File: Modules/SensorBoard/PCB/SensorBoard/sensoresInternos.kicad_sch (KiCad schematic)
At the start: 0 parts

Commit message: sensor board basic components
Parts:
- added U2: BMI160, Package_LGA:Bosch_LGA-14_3x2.5mm_P0.5mm, symbol Sensor_Motion:BMI160
- added U3: BME280, Package_LGA:Bosch_LGA-8_2.5x2.5mm_P0.65mm_ClockwisePinNumbering, symbol Sensor:BME280
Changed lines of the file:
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@@
 (kicad_sch
-	(version 20231120)
+	(version 20250114)
 	(generator "eeschema")
-	(generator_version "8.0")
+	(generator_version "9.0")
 	(paper "A4")
+	(symbol
+		(lib_id "Sensor:BME280")
+		(at 119.38 129.54 0)
+		(unit 1)
+		(exclude_from_sim no)
+		(in_bom yes)
+		(on_board yes)
+		(dnp no)
+		(fields_autoplaced yes)
+		(property "Reference" "U3"
+			(at 107.95 128.2699 0)
+			(effects
+				(font
+					(size 1.27 1.27)
+				)
+				(justify right)
+			)
+		)
+		(property "Value" "BME280"
+			(at 107.95 130.8099 0)
+			(effects
+				(font
+					(size 1.27 1.27)
+				)
+				(justify right)
+			)
+		)
+		(property "Footprint" "Package_LGA:Bosch_LGA-8_2.5x2.5mm_P0.65mm_ClockwisePinNumbering"
+			(at 157.48 140.97 0)
+			(effects
+				(font
+					(size 1.27 1.27)
+				)
+				(hide yes)
+			)
+		)
+		(property "Datasheet" "https://www.bosch-sensortec.com/media/boschsensortec/downloads/datasheets/bst-bme280-ds002.pdf"
+			(at 119.38 134.62 0)
+			(effects
+				(font
+					(size 1.27 1.27)
+				)
+				(hide yes)
+			)
+		)
+		(property "Description" "3-in-1 sensor, humidity, pressure, temperature, I2C and SPI interface, 1.71-3.6V, LGA-8"
+			(at 119.38 129.54 0)
+			(effects
+				(font
+					(size 1.27 1.27)
+				)
+				(hide yes)
+			)
+		)
+		(pin "3"
+		)
+		(pin "2"
+		)
+		(pin "7"
+		)
+		(pin "8"
+		)
+		(pin "1"
+		)
+		(pin "4"
+		)
+		(pin "5"
+		)
+		(pin "6"
+		)
+		(instances
+			(project ""
+				(path "/fa219048-dcb4-48ee-a6b6-8b1fad43a054/b6d62be8-6230-46e7-ab2b-f5043389658b"
+					(reference "U3")
+					(unit 1)
+				)
+			)
+		)
+	)
+	(symbol
+		(lib_id "Sensor_Motion:BMI160")
+		(at 120.65 67.31 0)
+		(unit 1)
+		(exclude_from_sim no)
+		(in_bom yes)
+		(on_board yes)
+		(dnp no)
+		(fields_autoplaced yes)
+		(property "Reference" "U2"
+			(at 122.7933 54.61 0)
+			(effects
+				(font
+					(size 1.27 1.27)
+				)
+				(justify left)
+			)
+		)
+		(property "Value" "BMI160"
+			(at 122.7933 57.15 0)
+			(effects
+				(font
+					(size 1.27 1.27)
+				)
+				(justify left)
+			)
+		)
+		(property "Footprint" "Package_LGA:Bosch_LGA-14_3x2.5mm_P0.5mm"
+			(at 120.65 67.31 0)
+			(effects
+				(font
+					(size 1.27 1.27)
+				)
+				(hide yes)
+			)
+		)
+		(property "Datasheet" "https://www.bosch-sensortec.com/media/boschsensortec/downloads/datasheets/bst-bmi160-ds000.pdf"
+			(at 102.87 45.72 0)
+			(effects
+				(font
+					(size 1.27 1.27)
+				)
+				(hide yes)
+			)
+		)
+		(property "Description" "Small, low power inertial measurement unit, LGA-14"
+			(at 120.65 67.31 0)
+			(effects
+				(font
+					(size 1.27 1.27)
+				)
+				(hide yes)
+			)
+		)
+		(pin "12"
+		)
+		(pin "3"
+		)
+		(pin "7"
+		)
+		(pin "4"
+		)
+		(pin "8"
+		)
+		(pin "1"
+		)
+		(pin "9"
+		)
+		(pin "11"
+		)
+		(pin "10"
+		)
+		(pin "6"
+		)
+		(pin "5"
+		)
+		(pin "2"
+		)
+		(pin "14"
+		)
+		(pin "13"
+		)
+		(instances
+			(project ""
+				(path "/fa219048-dcb4-48ee-a6b6-8b1fad43a054/b6d62be8-6230-46e7-ab2b-f5043389658b"
+					(reference "U2")
+					(unit 1)
+				)
+			)
+		)
+	)
 )

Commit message: Finished Supply board
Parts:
- removed U2: BMI160, Package_LGA:Bosch_LGA-14_3x2.5mm_P0.5mm, symbol Sensor_Motion:BMI160
- added C12, C13, C14, C15: 100nF, Capacitor_SMD:C_0603_1608Metric_Pad1.08x0.95mm_HandSolder, symbol Device:C_Small
- added JP2: BME280_Addr_Sel, Jumper:SolderJumper-3_P1.3mm_Open_RoundedPad1.0x1.5mm, symbol Jumper:SolderJumper_3_Open
- added U6: BMI160, Package_LGA:Bosch_LGA-14_3x2.5mm_P0.5mm, symbol Sensor_Motion:BMI160
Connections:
- net GND: now reaches U3.1 (GND)
- net GND: now also U3.7 (GND), C12.2, C13.2, C14.2, C15.2, JP2.3 (B), U6.6 (GNDIO), U6.7 (GND)
- net +3V3: now reaches U3.2 (CSB)
- net +3V3: now also U3.6 (VDDIO), U3.8 (VDD), C12.1, C13.1, C14.1, C15.1, JP2.1 (A), U6.5 (VDDIO), U6.8 (VDD)
- net I2C_BME.SDA: now reaches U3.3 (SDI)
- net I2C_BME.SCL: now reaches U3.4 (SCK)
- net at U3.5 (SDO): now also JP2.2 (C)
- new net SPI_IMU.CS0: U6.12 (CSB)
- new net SPI_IMU.MISO: U6.1 (SDO)
- new net SPI_IMU.MOSI: U6.14 (SDx)
- new net SPI_IMU.SCK: U6.13 (SCx)
- no-connect marks 0 -> 6

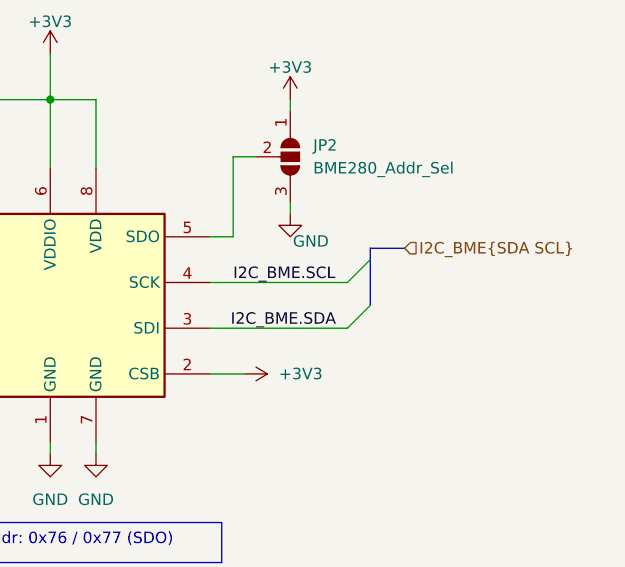
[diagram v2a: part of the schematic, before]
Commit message: Enrutado de diseño de PT100 en la sensorboard
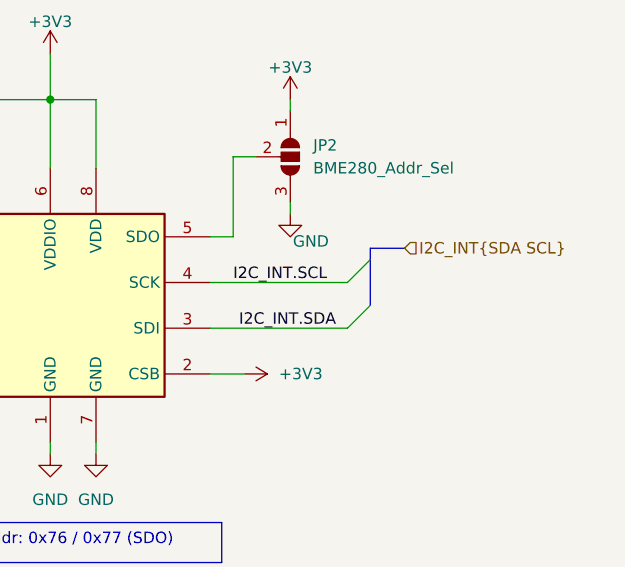
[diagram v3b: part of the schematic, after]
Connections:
- net I2C_BME.SCL renamed I2C_INT.SCL
- net I2C_BME.SDA renamed I2C_INT.SDA
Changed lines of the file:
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@@
 		)
 	)
-	(label "I2C_BME.SDA"
+	(label "I2C_INT.SDA"
 		(at 148.59 132.08 180)
 		(effects
@@
 		)
 	)
-	(label "I2C_BME.SCL"
+	(label "I2C_INT.SCL"
 		(at 137.16 127 0)
 		(effects
@@
 		)
 	)
-	(hierarchical_label "I2C_BME{SDA SCL}"
+	(hierarchical_label "I2C_INT{SDA SCL}"
 		(shape input)
 		(at 156.21 123.19 0)

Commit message: Finished Sensor and Backplane boards
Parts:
- added R15, R16: 10k, Resistor_SMD:R_0603_1608Metric_Pad0.98x0.95mm_HandSolder, symbol Device:R
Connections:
- net +3V3: now also R15.2, R16.2
- net I2C_INT.SCL: now also R16.1
- net I2C_INT.SDA: now also R15.1

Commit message: Working STM32, and SensorBoard: BME, BMI, PT100 and GPS
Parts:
- R15, R16: value 10k -> 2k2
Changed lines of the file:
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@@
 			)
 		)
-		(property "Value" "10k"
+		(property "Value" "2k2"
 			(at 165.1 122.555 90)
 			(effects
@@
 			)
 		)
-		(property "Value" "10k"
+		(property "Value" "2k2"
 			(at 168.91 122.555 90)
 			(effects
